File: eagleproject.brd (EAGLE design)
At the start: 100 x 80 mm, 0 parts

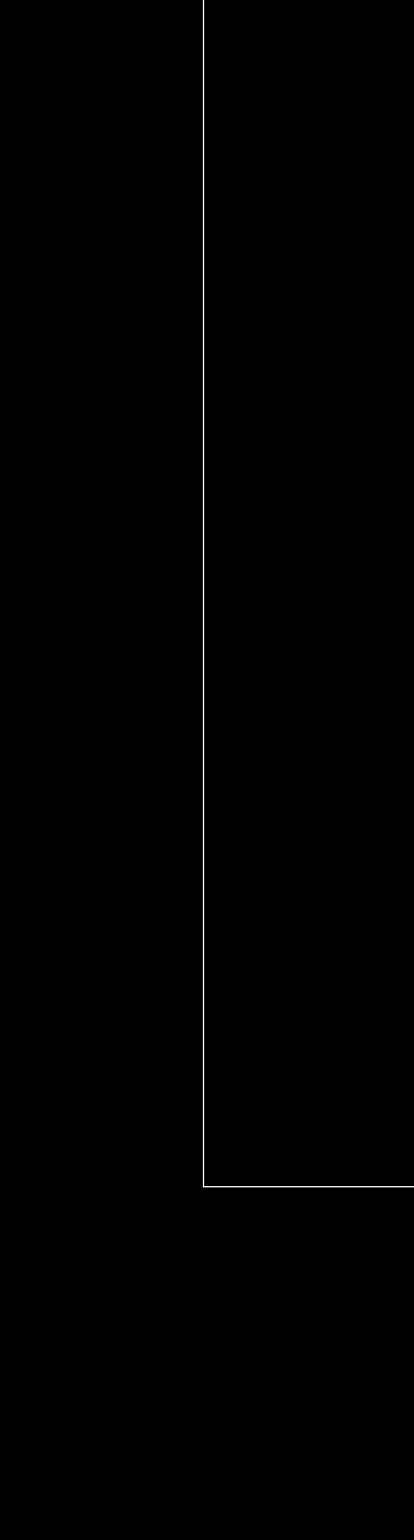
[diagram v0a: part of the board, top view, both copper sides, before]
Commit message: sparkfun libraries i didn't have
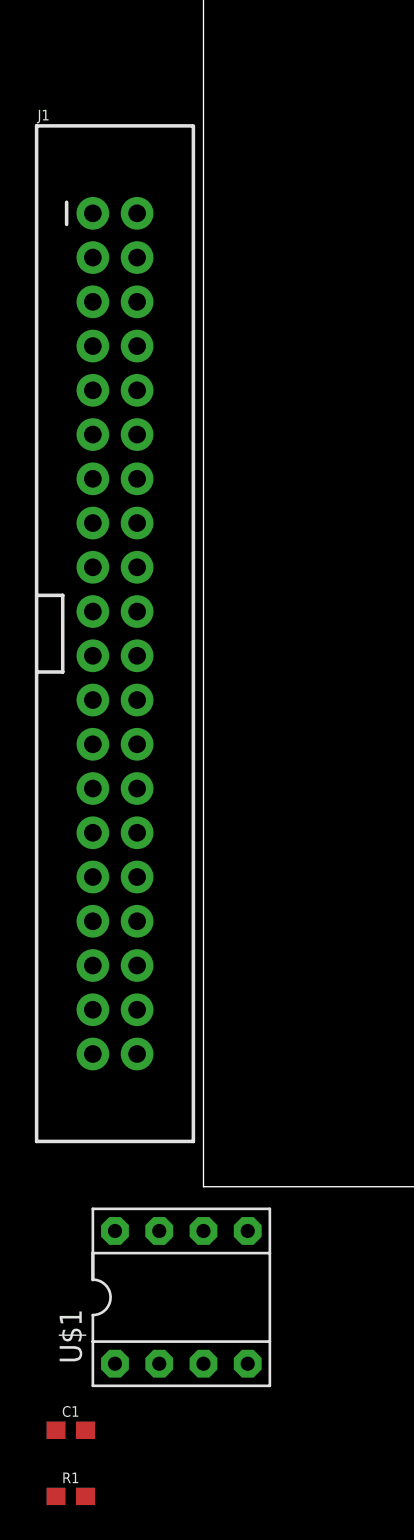
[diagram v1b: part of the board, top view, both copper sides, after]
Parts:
- added C1: 0.1uF, SparkFun-Capacitors:0603
- added J1: RASPBERRYPI-40-PIN-GPIO_PTH, SparkFun-Connectors:2X20_SHROUDED
- added R1: 100, SparkFun-Resistors:0603
- added U$1: MAX485DIL, SparkFun-Retired:DIL08
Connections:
- new net 3.3V: J1.1, J1.17
- new net 5V: C1.1, J1.2, J1.4, U$1.8
- new net A: R1.2, U$1.6
- new net B: R1.1, U$1.7
- new net GND: C1.2, J1.14, J1.20, J1.25, J1.30, J1.34, J1.39, J1.6, J1.9, U$1.5

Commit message: velleman user manual
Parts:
- added J2: XLR-3-FEMALE, SparkFun-Connectors:XLR-3_FEMALE
- added J3: XLR-3-MALE, SparkFun-Connectors:XLR-3_MALE
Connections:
- net A: now also J2.3, J3.3
- net B: now also J2.2, J3.2
- net GND: now also J2.1, J3.1
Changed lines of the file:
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@@
 <attribute name="VALUE" x="-7.62" y="-18.542" size="0.6096" layer="27" font="vector" ratio="20" align="top-center"/>
+</element>
+<element name="J2" library="SparkFun-Connectors" package="XLR-3_FEMALE" value="XLR-3-FEMALE" x="-22.86" y="-8.89" smashed="yes">
+<attribute name="NAME" x="-27.94" y="10.16" size="1.27" layer="25" font="vector"/>
+<attribute name="PROD_ID" value="CONN-14142" x="-22.86" y="-8.89" size="1.778" layer="27" font="vector" ratio="15" display="off"/>
+<attribute name="VALUE" x="-27.94" y="-17.78" size="1.27" layer="27" font="vector"/>
+</element>
+<element name="J3" library="SparkFun-Connectors" package="XLR-3_MALE" value="XLR-3-MALE" x="-49.53" y="-5.08" smashed="yes">
+<attribute name="NAME" x="-54.61" y="10.16" size="1.27" layer="25" font="vector"/>
+<attribute name="PROD_ID" value="CONN-14141" x="-49.53" y="-5.08" size="1.778" layer="27" font="vector" ratio="15" display="off"/>
+<attribute name="VALUE" x="-54.61" y="-17.78" size="1.27" layer="27" font="vector"/>
 </element>
 </elements>
@@
 </signal>
 <signal name="GND">
+<contactref element="C1" pad="2"/>
+<contactref element="U$1" pad="5"/>
+<contactref element="J2" pad="1"/>
+<contactref element="J3" pad="1"/>
+<contactref element="J1" pad="6"/>
 <contactref element="J1" pad="9"/>
+<contactref element="J1" pad="14"/>
+<contactref element="J1" pad="20"/>
 <contactref element="J1" pad="25"/>
-<contactref element="J1" pad="20"/>
-<contactref element="J1" pad="14"/>
-<contactref element="J1" pad="6"/>
 <contactref element="J1" pad="30"/>
 <contactref element="J1" pad="34"/>
 <contactref element="J1" pad="39"/>
-<contactref element="C1" pad="2"/>
-<contactref element="U$1" pad="5"/>
-<wire x1="-6.35" y1="45.72" x2="-3.81" y2="50.8" width="0" layer="19" extent="1-1"/>
-<wire x1="-3.81" y1="40.64" x2="-6.35" y2="45.72" width="0" layer="19" extent="1-1"/>
-<wire x1="-3.81" y1="33.02" x2="-3.81" y2="40.64" width="0" layer="19" extent="1-1"/>
-<wire x1="-6.35" y1="25.4" x2="-3.81" y2="33.02" width="0" layer="19" extent="1-1"/>
-<wire x1="-3.81" y1="20.32" x2="-6.35" y2="25.4" width="0" layer="19" extent="1-1"/>
-<wire x1="-3.81" y1="15.24" x2="-3.81" y2="20.32" width="0" layer="19" extent="1-1"/>
-<wire x1="-6.35" y1="7.62" x2="-3.81" y2="15.24" width="0" layer="19" extent="1-1"/>
-<wire x1="2.54" y1="-2.54" x2="-6.35" y2="7.62" width="0" layer="19" extent="1-1"/>
-<wire x1="-6.77" y1="-13.97" x2="2.54" y2="-2.54" width="0" layer="19" extent="1-1"/>
+<wire x1="-26.67" y1="-8.89" x2="-45.72" y2="-13.97" width="0" layer="19" extent="1-1"/>
+<wire x1="-6.77" y1="-13.97" x2="-26.67" y2="-8.89" width="0" layer="19" extent="1-1"/>
+<wire x1="2.54" y1="-2.54" x2="-6.77" y2="-13.97" width="0" layer="19" extent="1-1"/>
+<wire x1="-6.35" y1="7.62" x2="2.54" y2="-2.54" width="0" layer="19" extent="1-1"/>
+<wire x1="-3.81" y1="15.24" x2="-6.35" y2="7.62" width="0" layer="19" extent="1-1"/>
+<wire x1="-3.81" y1="20.32" x2="-3.81" y2="15.24" width="0" layer="19" extent="1-1"/>
+<wire x1="-6.35" y1="25.4" x2="-3.81" y2="20.32" width="0" layer="19" extent="1-1"/>
+<wire x1="-3.81" y1="33.02" x2="-6.35" y2="25.4" width="0" layer="19" extent="1-1"/>
+<wire x1="-3.81" y1="40.64" x2="-3.81" y2="33.02" width="0" layer="19" extent="1-1"/>
+<wire x1="-6.35" y1="45.72" x2="-3.81" y2="40.64" width="0" layer="19" extent="1-1"/>
+<wire x1="-3.81" y1="50.8" x2="-6.35" y2="45.72" width="0" layer="19" extent="1-1"/>
 </signal>
 <signal name="5V">
@@
 <contactref element="U$1" pad="7"/>
 <contactref element="R1" pad="1"/>
+<contactref element="J2" pad="2"/>
+<contactref element="J3" pad="2"/>
+<wire x1="-19.05" y1="-9.525" x2="-53.34" y2="-13.97" width="0" layer="19" extent="1-1"/>
+<wire x1="-8.47" y1="-17.78" x2="-19.05" y2="-9.525" width="0" layer="19" extent="1-1"/>
 <wire x1="-2.54" y1="-2.54" x2="-8.47" y2="-17.78" width="0" layer="19" extent="1-1"/>
 </signal>
@@
 <contactref element="R1" pad="2"/>
 <contactref element="U$1" pad="6"/>
+<contactref element="J2" pad="3"/>
+<contactref element="J3" pad="3"/>
+<wire x1="-22.86" y1="-13.335" x2="-49.53" y2="-13.97" width="0" layer="19" extent="1-1"/>
+<wire x1="-6.77" y1="-17.78" x2="-22.86" y2="-13.335" width="0" layer="19" extent="1-1"/>
 <wire x1="0" y1="-2.54" x2="-6.77" y2="-17.78" width="0" layer="19" extent="1-1"/>
 </signal>

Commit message: first version for manufacturing
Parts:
- added J4: (no value), SparkFun-Connectors:1X05
- added U$2: (no value), diamondimage#jpeg:DIAMONDIMAGE#JPEG
- added U$3: (no value), nameforpcb#jpg2:NAMEFORPCB#JPG
- J3: value XLR-3-MALE -> (none); device SparkFun-Connectors:XLR-3_MALE -> SparkFun-Connectors:1X04
- moved J3 91.8 mm to (19.1, 55.9)
- moved R1 85.4 mm to (50.8, 44.5), turned to 90 degrees
- moved J2 83.2 mm to (57.1, 14.0), turned to 180 degrees
- moved C1 80.2 mm to (53.3, 38.1)
- moved U$1 77.4 mm to (57.1, 44.5), turned to 90 degrees
- moved J1 73.6 mm to (57.1, 71.1), turned to 90 degrees
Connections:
- new net DI: J1.29, U$1.4
- new net MISO: J1.21, J4.3
- new net MOSI: J1.19, J4.2
- new net SCL: J1.5, J3.4
- new net SCLK: J1.23, J4.4
- new net SDA: J1.3, J3.3
- net 3.3V: now also J3.2, J4.5
- net 5V: now also U$1.3
- net A: no longer J3.3
- net B: no longer J3.2
- net GND: now also J4.1, U$1.1, U$1.2
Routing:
- net 5V: track 0.00 -> 109.0 mm
- net 3.3V: track 0.00 -> 99.2 mm
- net SCLK: track 0.00 -> 44.8 mm, vias 0 -> 1
- net MISO: track 0.00 -> 44.0 mm, vias 0 -> 1
- net MOSI: track 0.00 -> 43.3 mm, vias 0 -> 1
- net A: track 0.00 -> 37.2 mm
- net B: track 0.00 -> 36.7 mm
- net DI: track 0.00 -> 24.7 mm
- net SDA: track 0.00 -> 18.7 mm
- net SCL: track 0.00 -> 18.7 mm
- added copper zone on layer 1, net GND
- added copper zone on layer 16, net GND
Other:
- board size 100 x 80 mm -> 101.6 x 76.2 mm
